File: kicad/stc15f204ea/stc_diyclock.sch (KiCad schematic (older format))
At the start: 57 parts, among them J1 JACK_2P, K1 DC5V, P1 4Pin, P1001 CONN_01X04, P2 3Pin, P3 2Pin, Q1 8550, Q2 8550, Q3 8550, Q4 8550, Q5 8550, Q6 8550, SW1 SW_PUSH, SW2 SW_PUSH, U1 DS1302, U2 STC15F204EA, Y1 32768

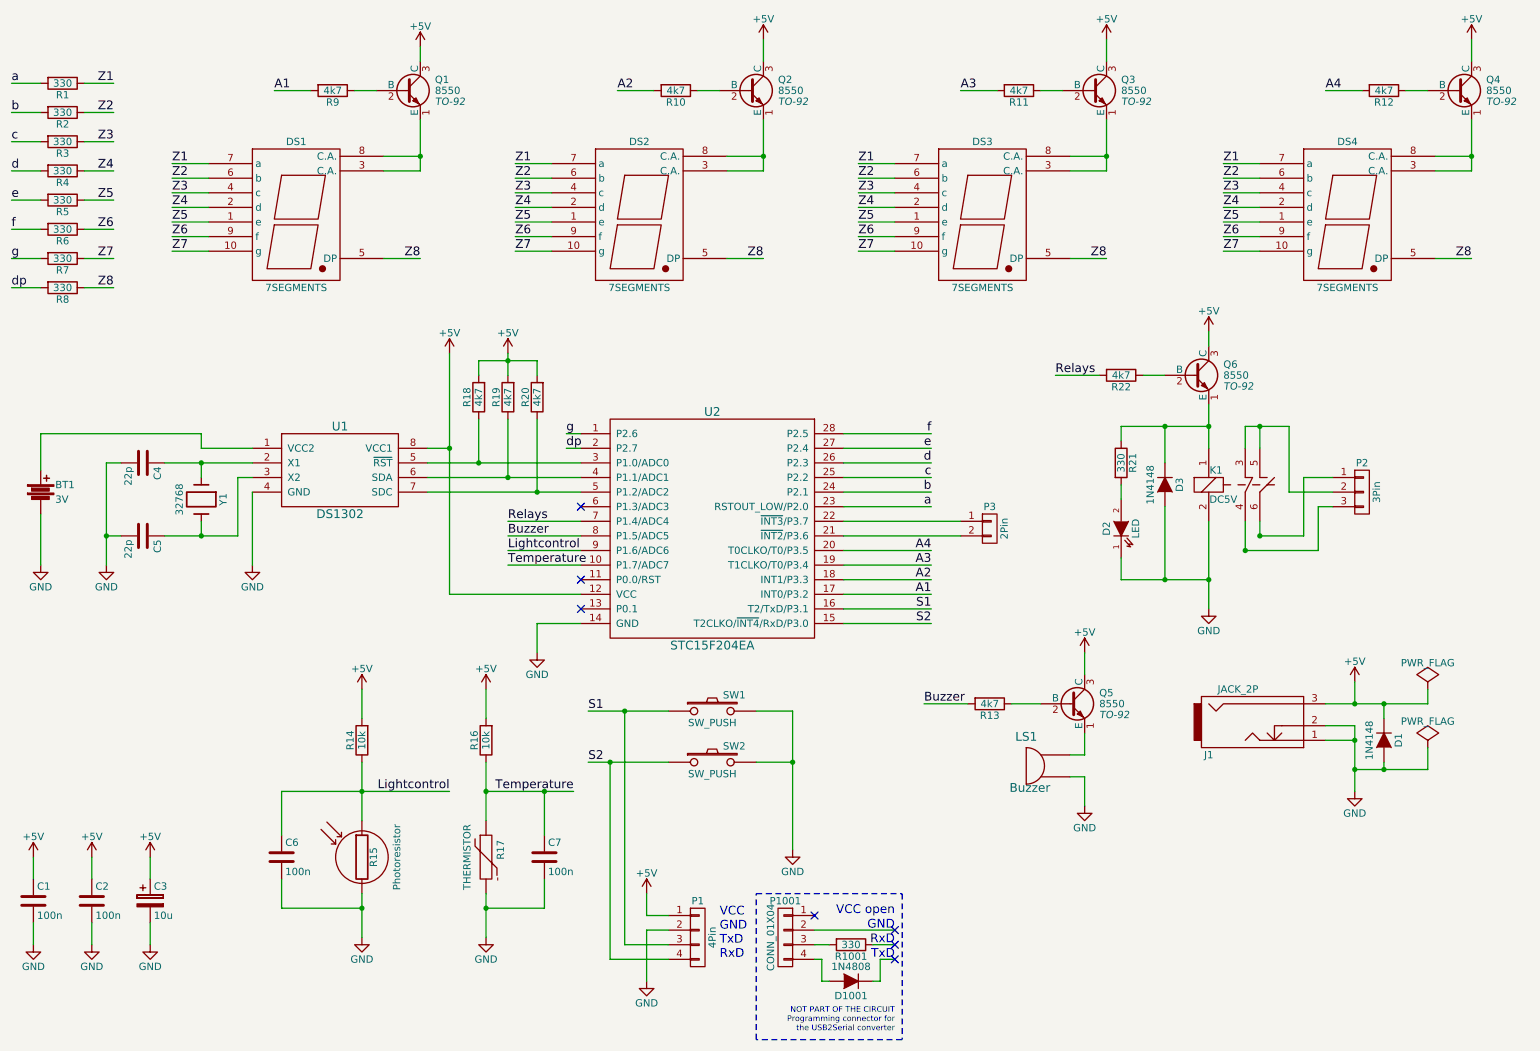
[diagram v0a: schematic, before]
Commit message: fix for schematics (programming connector and transistors)
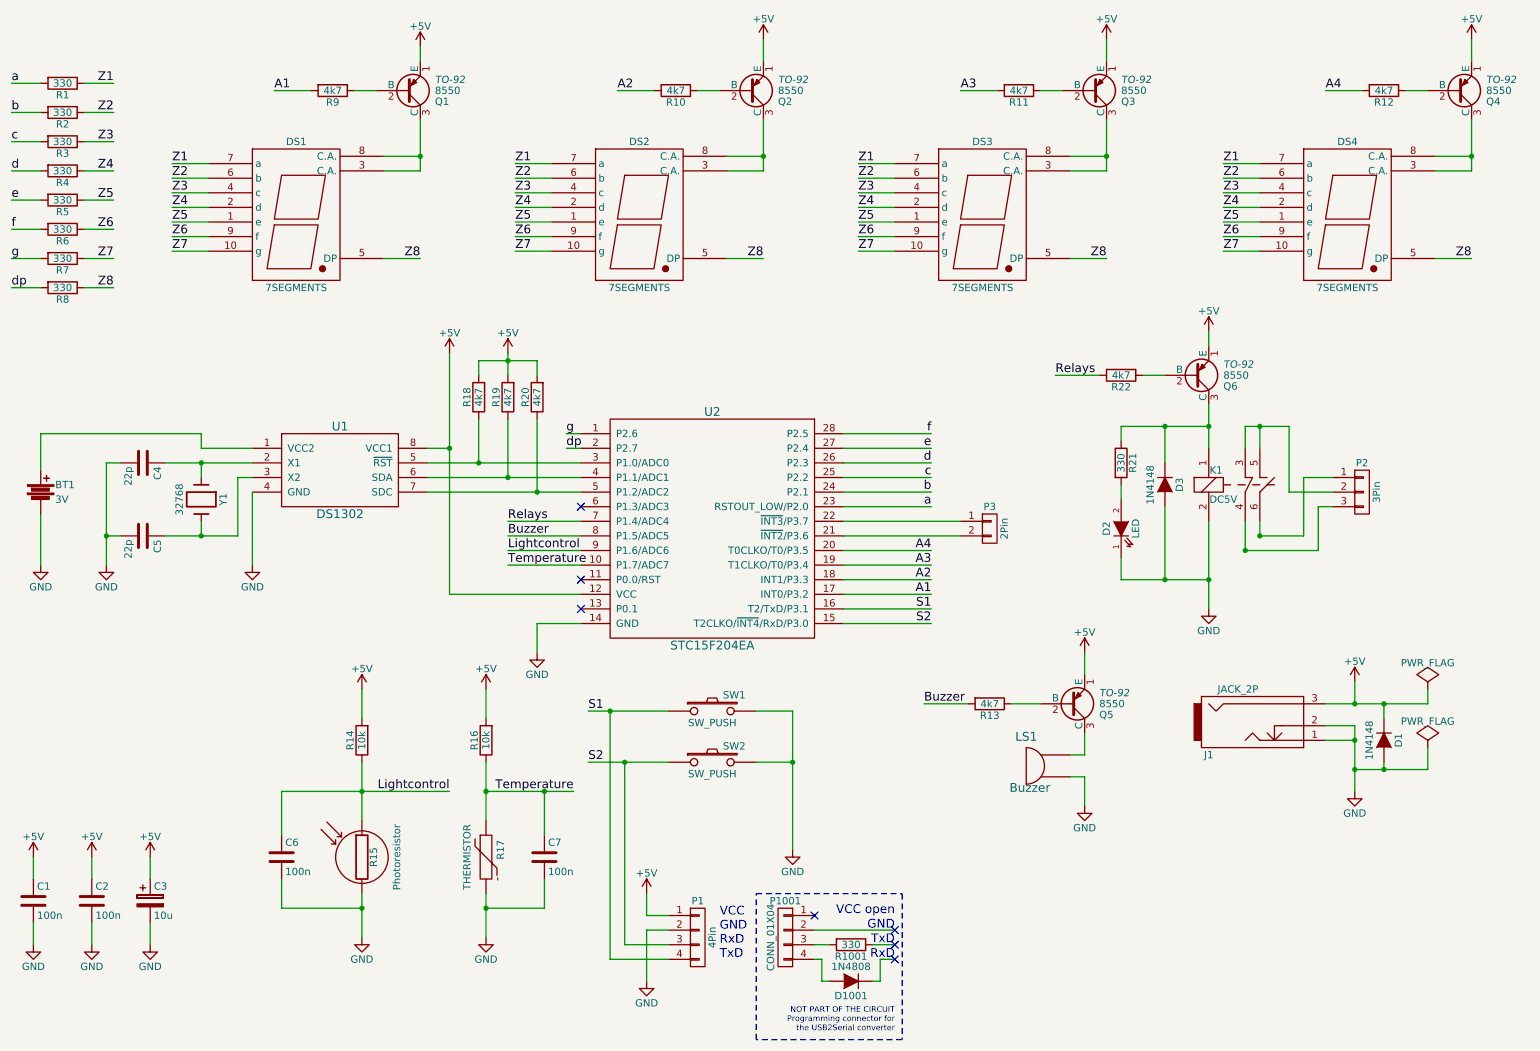
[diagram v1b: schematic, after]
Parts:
- removed Q1, Q2, Q3, Q4, Q5, Q6: 8550, TO-92, symbol S8050
- added Q1, Q2, Q3, Q4, Q5, Q6: 8550, TO-92, symbol S8550
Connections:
- net +5V: now also Q1.1 (E), Q2.1 (E), Q3.1 (E), Q4.1 (E), Q5.1 (E), Q6.1 (E)
- net S1: now also P1.4 (P4); no longer P1.3 (P3)
- net S2: now also P1.3 (P3); no longer P1.4 (P4)
- net at DS1.3 (C.A.), DS1.8 (C.A.): now also Q1.3 (C)
- net at DS2.3 (C.A.), DS2.8 (C.A.): now also Q2.3 (C)
- net at DS3.3 (C.A.), DS3.8 (C.A.): now also Q3.3 (C)
- net at DS4.3 (C.A.), DS4.8 (C.A.): now also Q4.3 (C)
- net at R9.1: now also Q1.2 (B)
- net at R10.1: now also Q2.2 (B)
- net at R11.1: now also Q3.2 (B)
- net at R12.1: now also Q4.2 (B)
- net at R13.1: now also Q5.2 (B)
- net at D3.1 (K), K1.1, R21.1: now also Q6.3 (C)
- net at R22.1: now also Q6.2 (B)
- new net: LS1.~, Q5.3 (C)
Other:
- note added: "VCC\nGND\nRxD\nTxD"
- note removed: "VCC\nGND\nTxD\nRxD"
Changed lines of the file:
@@
 LIBS:contrib
 LIBS:valves
+LIBS:stc_diyclock-cache
 EELAYER 25 0
 EELAYER END
@@
 Sheet 1 1
 Title "STC DIYCLOCK (STC Do It Yourself Clock)"
-Date "2017-03-04"
-Rev "01"
+Date "2017-03-18"
+Rev "02"
 Comp "KKmoon Compact Digital 4-digit LED Clock DIY Kit"
 Comment1 "Sold on Bangood"
@@
 $EndComp
 Text Notes 5600 7150 0    60   ~ 0
-VCC\nGND\nTxD\nRxD
+VCC\nGND\nRxD\nTxD
 $Comp
 L CONN_01X04 P1001
@@
 $EndComp
 $Comp
-L S8050 Q1
-U 1 1 58BAE150
-P 3450 1200
-F 0 "Q1" H 3650 1275 50  0000 L CNN
-F 1 "8550" H 3650 1200 50  0000 L CNN
-F 2 "TO-92" H 3650 1125 50  0000 L CIN
-F 3 "" H 3450 1200 50  0000 L CNN
-	1    3450 1200
-	1    0    0    -1
-$EndComp
-$Comp
-L S8050 Q2
-U 1 1 58BAE3FD
-P 5800 1200
-F 0 "Q2" H 6000 1275 50  0000 L CNN
-F 1 "8550" H 6000 1200 50  0000 L CNN
-F 2 "TO-92" H 6000 1125 50  0000 L CIN
-F 3 "" H 5800 1200 50  0000 L CNN
-	1    5800 1200
-	1    0    0    -1
-$EndComp
-$Comp
-L S8050 Q3
-U 1 1 58BAE4C6
-P 8150 1200
-F 0 "Q3" H 8350 1275 50  0000 L CNN
-F 1 "8550" H 8350 1200 50  0000 L CNN
-F 2 "TO-92" H 8350 1125 50  0000 L CIN
-F 3 "" H 8150 1200 50  0000 L CNN
-	1    8150 1200
-	1    0    0    -1
-$EndComp
-$Comp
-L S8050 Q4
-U 1 1 58BAE5A0
-P 10650 1200
-F 0 "Q4" H 10850 1275 50  0000 L CNN
-F 1 "8550" H 10850 1200 50  0000 L CNN
-F 2 "TO-92" H 10850 1125 50  0000 L CIN
-F 3 "" H 10650 1200 50  0000 L CNN
-	1    10650 1200
-	1    0    0    -1
-$EndComp
-$Comp
 L R R19
 U 1 1 58BAEDBB
@@
 $EndComp
 $Comp
-L S8050 Q5
-U 1 1 58BB1A64
-P 8000 5400
-F 0 "Q5" H 8200 5475 50  0000 L CNN
-F 1 "8550" H 8200 5400 50  0000 L CNN
-F 2 "TO-92" H 8200 5325 50  0000 L CIN
-F 3 "" H 8000 5400 50  0000 L CNN
-	1    8000 5400
-	1    0    0    -1
-$EndComp
-$Comp
-L S8050 Q6
-U 1 1 58BB1BA1
-P 8850 3150
-F 0 "Q6" H 9050 3225 50  0000 L CNN
-F 1 "8550" H 9050 3150 50  0000 L CNN
-F 2 "TO-92" H 9050 3075 50  0000 L CIN
-F 3 "" H 8850 3150 50  0000 L CNN
-	1    8850 3150
-	1    0    0    -1
-$EndComp
-$Comp
 L D D3
 U 1 1 58BB1F6B
@@
 Wire Wire Line
 	5100 6950 5100 7300
-Wire Wire Line
-	4950 7050 5250 7050
-Wire Wire Line
-	4950 5450 4950 7050
-Connection ~ 4950 5450
-Wire Wire Line
-	4850 7150 5250 7150
-Wire Wire Line
-	4850 5800 4850 7150
-Connection ~ 4850 5800
 Connection ~ 3150 6000
 Wire Wire Line
@@
 GND
 Text Notes 6800 7050 2    60   ~ 0
+TxD
+Text Notes 6800 7150 2    60   ~ 0
 RxD
-Text Notes 6800 7150 2    60   ~ 0
-TxD
 NoConn ~ 4650 4050
 NoConn ~ 4650 4550
@@
 Wire Wire Line
 	9500 3950 9500 3500
+$Comp
+L S8550 Q1
+U 1 1 58CD2324
+P 3450 1200
+F 0 "Q1" H 3650 1275 50  0000 L CNN
+F 1 "8550" H 3650 1200 50  0000 L CNN
+F 2 "TO-92" H 3650 1125 50  0000 L CIN
+F 3 "" H 3450 1200 50  0000 L CNN
+	1    3450 1200
+	1    0    0    1
+$EndComp
+$Comp
+L S8550 Q2
+U 1 1 58CD4A70
+P 5800 1200
+F 0 "Q2" H 6000 1275 50  0000 L CNN
+F 1 "8550" H 6000 1200 50  0000 L CNN
+F 2 "TO-92" H 6000 1125 50  0000 L CIN
+F 3 "" H 5800 1200 50  0000 L CNN
+	1    5800 1200
+	1    0    0    1
+$EndComp
+$Comp
+L S8550 Q3
+U 1 1 58CD4B7D
+P 8150 1200
+F 0 "Q3" H 8350 1275 50  0000 L CNN
+F 1 "8550" H 8350 1200 50  0000 L CNN
+F 2 "TO-92" H 8350 1125 50  0000 L CIN
+F 3 "" H 8150 1200 50  0000 L CNN
+	1    8150 1200
+	1    0    0    1
+$EndComp
+$Comp
+L S8550 Q4
+U 1 1 58CD4C57
+P 10650 1200
+F 0 "Q4" H 10850 1275 50  0000 L CNN
+F 1 "8550" H 10850 1200 50  0000 L CNN
+F 2 "TO-92" H 10850 1125 50  0000 L CIN
+F 3 "" H 10650 1200 50  0000 L CNN
+	1    10650 1200
+	1    0    0    1
+$EndComp
+$Comp
+L S8550 Q5
+U 1 1 58CD5115
+P 8000 5400
+F 0 "Q5" H 8200 5475 50  0000 L CNN
+F 1 "8550" H 8200 5400 50  0000 L CNN
+F 2 "TO-92" H 8200 5325 50  0000 L CIN
+F 3 "" H 8000 5400 50  0000 L CNN
+	1    8000 5400
+	1    0    0    1
+$EndComp
+$Comp
+L S8550 Q6
+U 1 1 58CD524B
+P 8850 3150
+F 0 "Q6" H 9050 3225 50  0000 L CNN
+F 1 "8550" H 9050 3150 50  0000 L CNN
+F 2 "TO-92" H 9050 3075 50  0000 L CIN
+F 3 "" H 8850 3150 50  0000 L CNN
+	1    8850 3150
+	1    0    0    1
+$EndComp
+Wire Wire Line
+	5250 7050 4950 7050
+Wire Wire Line
+	4950 7050 4950 5800
+Connection ~ 4950 5800
+Wire Wire Line
+	5250 7150 4850 7150
+Wire Wire Line
+	4850 7150 4850 5450
+Connection ~ 4850 5450
 $EndSCHEMATC
